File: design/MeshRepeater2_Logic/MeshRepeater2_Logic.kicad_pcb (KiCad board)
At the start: 2 copper layers, 90 x 60 mm, 57 parts, among them J10 AVR ISP 3V3, J11 LC OUT - SYS 3V3, J13 SMA 50Ohm, J201 INTERBOARD 2x6 VERTICAL, J3 I2C3V3, J4 GPS / T114 P3, J5 UART3V3, M1 NiceNano_CLONE_MODIFIED, M2 HT-RA62, Q2 AO3401A, Q3 2N7002K, SW1 USER, SW2 RESET, U4 DS3231MZ+TRL, U6 ATtiny13A-SSU, U7 SN74LVC2G125

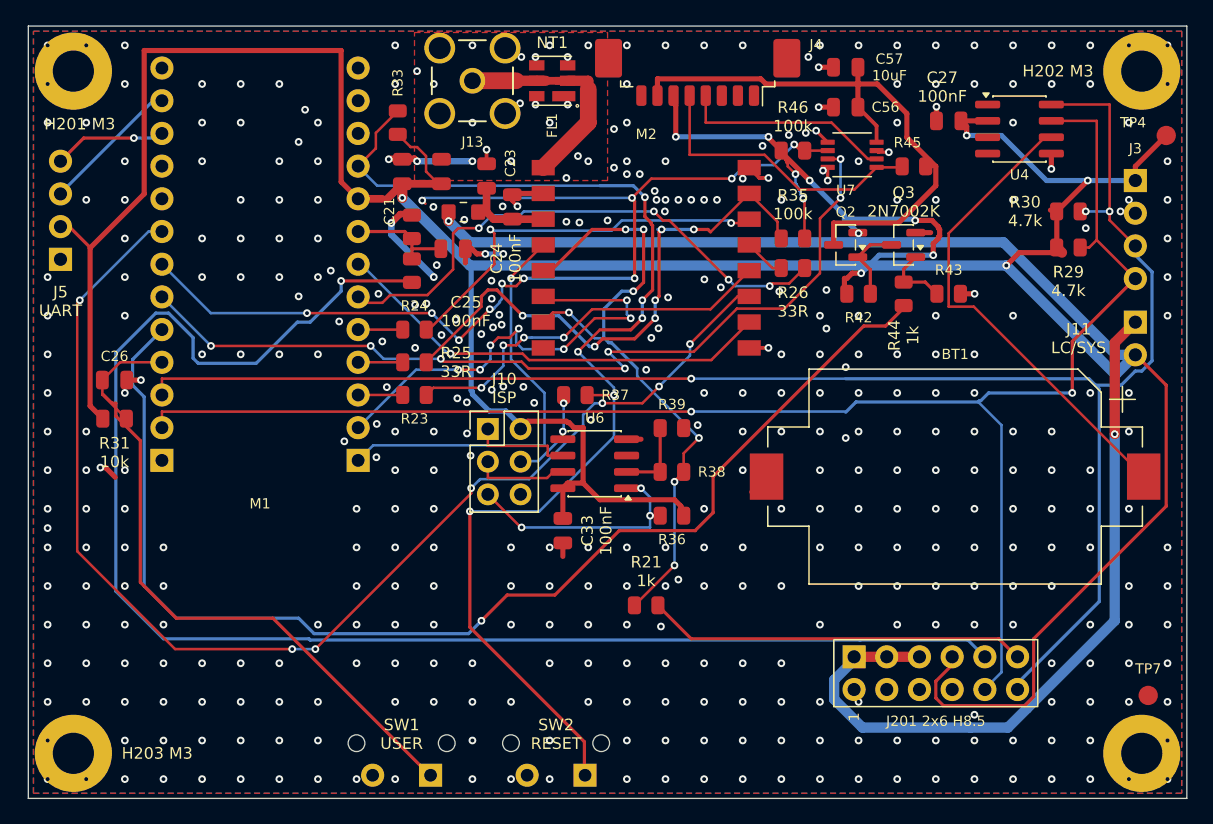
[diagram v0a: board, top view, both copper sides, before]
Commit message: Publish Mesh Repeater 2.0 A3 prototype and engineering audit
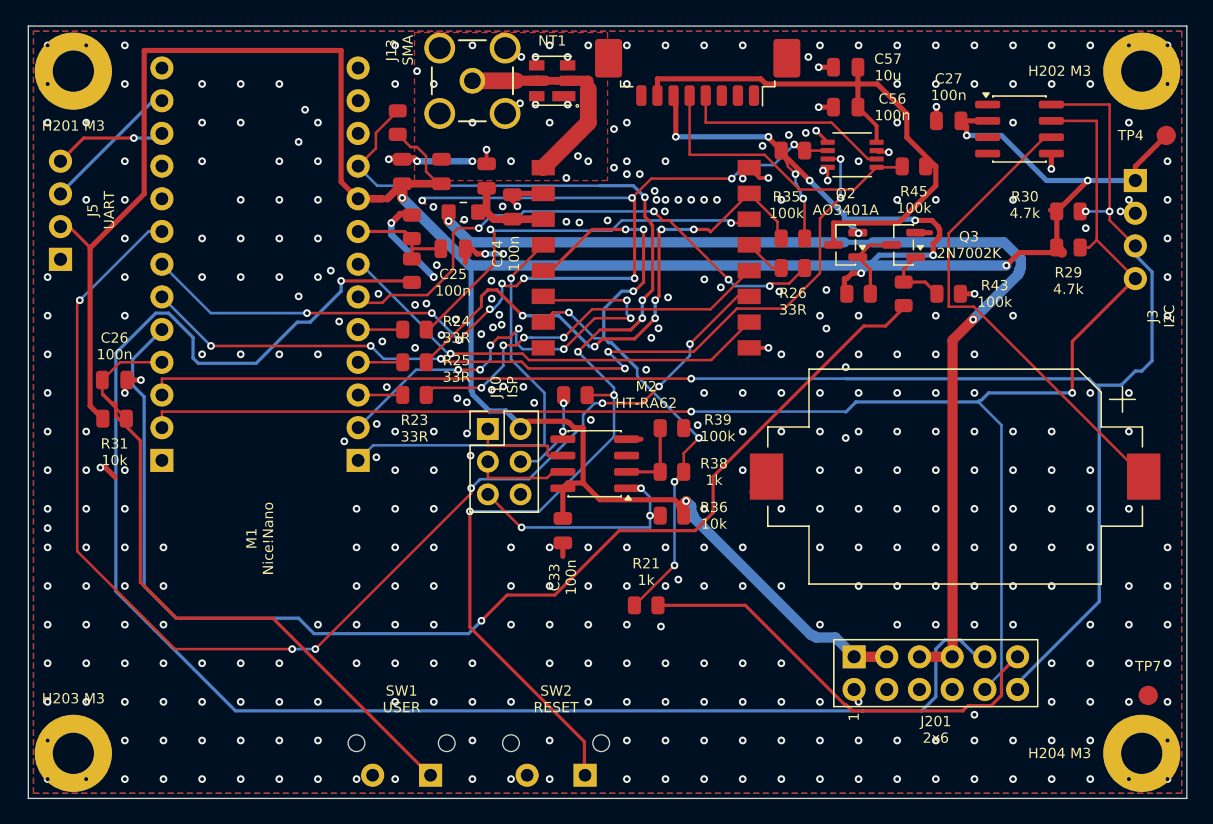
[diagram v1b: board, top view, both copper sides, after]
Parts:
- removed J11: LC OUT - SYS 3V3, Meshcore:Connfly_DS1022_1x02RUF11_B_Horizontal__V2_J11
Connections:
- net /RADIO_3V3 renamed /RADIO_LOCAL_3V3
- FB1 pad 1: SYS_3V3 -> RADIO_3V3
- J201 pad 1: FILTER_OUT -> SYS_3V3
- J201 pad 3: FILTER_OUT -> SYS_3V3
- J201 pad 5: FILTER_OUT -> RADIO_3V3
- J201 pad 7: SYS_3V3 -> RADIO_3V3
- J201 pad 8: GND -> unconnected-(J201-NC-Pad8)
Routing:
- net SYS_3V3: track 360.1 -> 265.2 mm
- net RADIO_3V3: track 0.00 -> 82.0 mm, vias 0 -> 2
- net FILTER_OUT: track 59.0 -> 0.00 mm, vias 1 -> 0
- net BAT: track 118.1 -> 124.8 mm
- net MODE: track 29.6 -> 34.1 mm
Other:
- board text added: "1RF 2GND"
- board text added: "C21 10u"
- board text added: "C22 100n"
- board text added: "C23 22u"
- board text added: "C24 100n"
- board text added: "C25 100n"
- board text added: "C26 100n"
- board text added: "C27 100n"
- board text added: "C33 100n"
- board text added: "C56 100n"
- board text added: "C57 10u"
- board text added: "FB1 60R"
- board text added: "FL1 S869M000 S003"
- board text added: "J10 ISP 1 MISO 2 3V3 3 SCK 4 MOSI 5 RST 6 GND"
- board text added: "J201 1/3 SYS 5/7 RADIO 2/4/6 GND 8 NC 9 BAT 10 SDA 11 MODE 12 SCL"
- board text added: "J201 2x6"
- board text added: "J3 I2C 1 3V3 2 GND 3 SCL 4 SDA"
- board text added: "J4 GPS 1 NC 2 NC 3 NC 4 RX 5 TX 6 BACKUP 7 POWER 8 GND"
- board text added: "J5 UART 1 GND 2 3V3 3 TX 4 RX"
- board text added: "M1 Nice!Nano"
- board text added: "U7 74LVC 2G125"
- board text added: "USB: снять J11 на POWER"
- board text removed: "1"
- board text removed: "1 GND"
- board text removed: "1 MISO"
- board text removed: "1 VIN"
- board text removed: "1/3/5 OUT | 2/4/6/8 GND"
- board text removed: "11 MODE | 12 SCL"
- board text removed: "2"
- board text removed: "2 GND"
- board text removed: "2 VIN"
- board text removed: "3"
- board text removed: "3 SCK"
- board text removed: "3 SCL"
- board text removed: "3 TX"
- board text removed: "4"
- board text removed: "4 MOSI"
- board text removed: "4 RX"
- board text removed: "4 SDA"
- board text removed: "5"
- board text removed: "5 RESET"
- board text removed: "6"
- board text removed: "6 GND"
- board text removed: "7"
- board text removed: "7 3V3 | 9 BAT | 10 SDA"
- board text removed: "8"
- board text removed: "BT1"
- board text removed: "C21"
- board text removed: "C21 10uF"
- board text removed: "C22 100nF"
- board text removed: "C23"
- board text removed: "C23 22uF"
- board text removed: "C24 100nF"
- board text removed: "C25 100nF"
- board text removed: "C26"
- board text removed: "C26 100nF"
- board text removed: "C27 100nF"
- board text removed: "C33 100nF"
- board text removed: "C56"
- board text removed: "C56 100nF"
- board text removed: "C57 10uF"
- board text removed: "D3 CHARGE D4 DONE"
- board text removed: "FB1 60R@100MHz"
- board text removed: "FL1"
- board text removed: "FL1 S869M000S003"
- board text removed: "G1 x1.5"
- board text removed: "G2 x1.5"
- board text removed: "G3 x2"
- board text removed: "G4 x1.5"
- board text removed: "G5 x1.5"
- board text removed: "G6 x1.5"
- board text removed: "G7 x1.5"
- board text removed: "J11 LC / SYS 1 LC_OUT 2 SYS_3V3"
- board text removed: "J11 LC/SYS"
- board text removed: "J13"
- board text removed: "J13 SMA 1 RF 2 GND"
- board text removed: "J201 2x6 H8.5"
- board text removed: "J3"
- board text removed: "J4"
- board text removed: "J4 GPS 1 NC/RST 2 NC/PPS 3 NC/WAKE 4 RX 5 TX 6 BACKUP 7 POWER 8 GND"
- board text removed: "M1"
- board text removed: "M1 NiceNano"
- board text removed: "M2"
- board text removed: "Q2"
- board text removed: "R23"
- board text removed: "R24"
- board text removed: "R33"
- board text removed: "R36"
- board text removed: "R37"
- board text removed: "R38"
- board text removed: "R39"
- board text removed: "R42"
- board text removed: "R43"
- board text removed: "R45"
- board text removed: "REMOVE J11 BEFORE USB"
- board text removed: "U4"
- board text removed: "U6"
- board text removed: "U7"
- board text removed: "U7 SN74LVC2G125"
- board text removed: "USB"

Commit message: Publish Mesh Repeater 2.0 A4 with consistent silkscreen and clean current CAD
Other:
- board text added: "1 GND 2 3V3 3 TX 4 RX"
- board text added: "R27 2M2"
- board text added: "R28 2M2"
- board text added: "R29 4k7"
- board text added: "R30 4k7"
- board text added: "RF"
- board text added: "U7 74LVC2G125"
- board text removed: "J10 ISP"
- board text removed: "J201 2x6"
- board text removed: "J3 I2C"
- board text removed: "J4 GPS"
- board text removed: "J5 UART 1 GND 2 3V3 3 TX 4 RX"
- board text removed: "R27 2.2M"
- board text removed: "R28 2.2M"
- board text removed: "R29 4.7k"
- board text removed: "R30 4.7k"
- board text removed: "U7 74LVC 2G125"

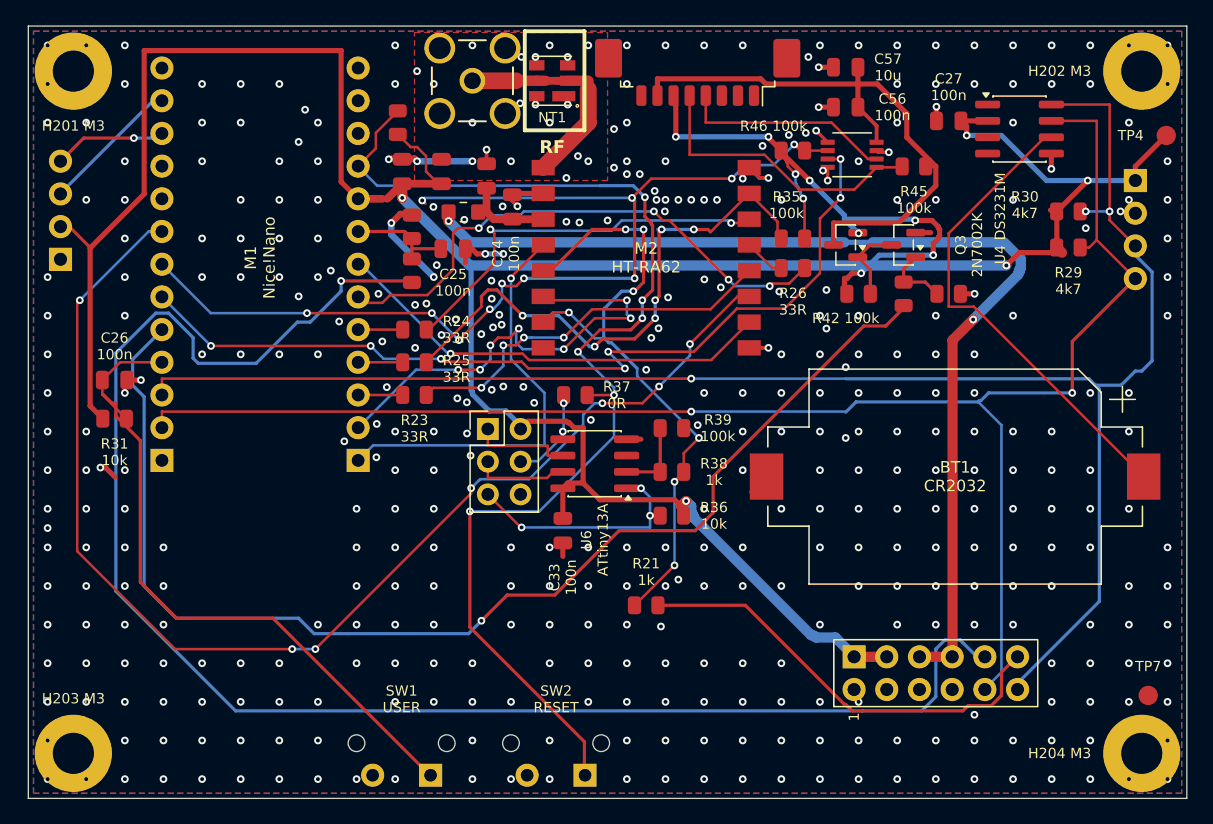
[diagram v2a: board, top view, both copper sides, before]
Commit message: Publish A5 routing fixes and CC BY-NC-SA licensing
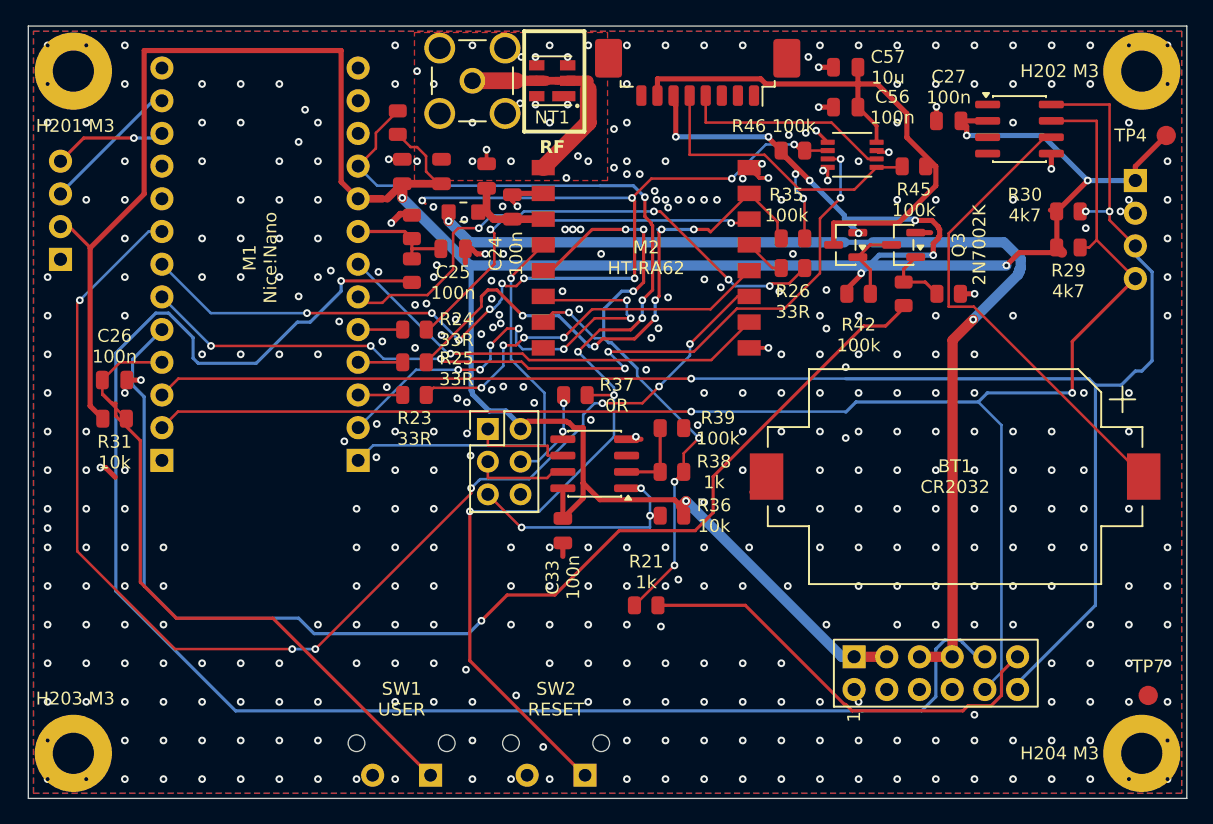
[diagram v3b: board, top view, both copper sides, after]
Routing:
- net GND: track 43.9 -> 30.4 mm, vias 423 -> 428
- net SCL: track 133.6 -> 132.6 mm
- net SDA: track 125.7 -> 124.9 mm
- net SYS_3V3: track 265.2 -> 265.9 mm
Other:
- board text added: "1 3V3 2 GND 3 SCL 4 SDA"
- board text added: "1 RF 2 GND"
- board text added: "60R"
- board text added: "FB1"
- board text added: "FL1 S869 M000 S003"
- board text added: "J3 I2C"
- board text removed: "1RF 2GND"
- board text removed: "FB1 60R"
- board text removed: "FL1 S869M000 S003"
- board text removed: "J3 I2C 1 3V3 2 GND 3 SCL 4 SDA"
